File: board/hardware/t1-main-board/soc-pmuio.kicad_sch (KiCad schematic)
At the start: 28 parts, among them U1301 RK3566, Y1301 24 MHz

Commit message: Board: capture blk.debug
Debug UART2 (1.8 V) and I2S/DSD pads with ground pads, reset, PMIC and
power-key pads (PCB-T-09), a pad on every spare SoC GPIO whose pinout v1
row names one (the DEBUG bus, on the SoC's right edge), and a rail pad
for each power-tree rail no other sheet probes (PCB-T-02). Each DAC
sheet carries a pad on its MCLK. The spares pinout v1 leaves without a
pad now carry no-connect flags. On the root, facing sheet pins are
joined directly only where the route meets no other symbol.

Co-Authored-By: Claude Opus 5.5 <noreply@anthropic.com>
Claude-Session: https://claude.ai/code/session_01Ei262h3TpgY9vyfNLMi5Mn
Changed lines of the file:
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@@
 (label "EFUSE_VBUS_IMON" (at 132.08 203.2 90) (effects (font (size 1.27 1.27)) (justify left bottom)))
 (bus (pts (xy 45.72 252.73) (xy 50.8 252.73)) (stroke (width 0) (type default)))
-(hierarchical_label "{FP}" (shape bidirectional) (at 45.72 252.73 180) (effects (font (size 1.27 1.27)) (justify right)))
+(hierarchical_label "{DEBUG}" (shape bidirectional) (at 45.72 252.73 180) (effects (font (size 1.27 1.27)) (justify right)))
 (bus (pts (xy 76.2 252.73) (xy 81.28 252.73)) (stroke (width 0) (type default)))
-(hierarchical_label "{I2C0}" (shape bidirectional) (at 76.2 252.73 180) (effects (font (size 1.27 1.27)) (justify right)))
+(hierarchical_label "{FP}" (shape bidirectional) (at 76.2 252.73 180) (effects (font (size 1.27 1.27)) (justify right)))
 (bus (pts (xy 106.68 252.73) (xy 111.76 252.73)) (stroke (width 0) (type default)))
-(hierarchical_label "{I2C1}" (shape bidirectional) (at 106.68 252.73 180) (effects (font (size 1.27 1.27)) (justify right)))
+(hierarchical_label "{I2C0}" (shape bidirectional) (at 106.68 252.73 180) (effects (font (size 1.27 1.27)) (justify right)))
 (bus (pts (xy 137.16 252.73) (xy 142.24 252.73)) (stroke (width 0) (type default)))
-(hierarchical_label "{I2C2}" (shape bidirectional) (at 137.16 252.73 180) (effects (font (size 1.27 1.27)) (justify right)))
+(hierarchical_label "{I2C1}" (shape bidirectional) (at 137.16 252.73 180) (effects (font (size 1.27 1.27)) (justify right)))
 (bus (pts (xy 167.64 252.73) (xy 172.72 252.73)) (stroke (width 0) (type default)))
-(hierarchical_label "{IMON}" (shape bidirectional) (at 167.64 252.73 180) (effects (font (size 1.27 1.27)) (justify right)))
+(hierarchical_label "{I2C2}" (shape bidirectional) (at 167.64 252.73 180) (effects (font (size 1.27 1.27)) (justify right)))
 (bus (pts (xy 198.12 252.73) (xy 203.2 252.73)) (stroke (width 0) (type default)))
-(hierarchical_label "{IO_IRQ}" (shape bidirectional) (at 198.12 252.73 180) (effects (font (size 1.27 1.27)) (justify right)))
+(hierarchical_label "{IMON}" (shape bidirectional) (at 198.12 252.73 180) (effects (font (size 1.27 1.27)) (justify right)))
 (bus (pts (xy 228.6 252.73) (xy 233.68 252.73)) (stroke (width 0) (type default)))
-(hierarchical_label "{KEYS}" (shape bidirectional) (at 228.6 252.73 180) (effects (font (size 1.27 1.27)) (justify right)))
+(hierarchical_label "{IO_IRQ}" (shape bidirectional) (at 228.6 252.73 180) (effects (font (size 1.27 1.27)) (justify right)))
 (bus (pts (xy 259.08 252.73) (xy 264.16 252.73)) (stroke (width 0) (type default)))
-(hierarchical_label "{NFC}" (shape bidirectional) (at 259.08 252.73 180) (effects (font (size 1.27 1.27)) (justify right)))
+(hierarchical_label "{KEYS}" (shape bidirectional) (at 259.08 252.73 180) (effects (font (size 1.27 1.27)) (justify right)))
 (bus (pts (xy 45.72 245.11) (xy 50.8 245.11)) (stroke (width 0) (type default)))
-(hierarchical_label "{PMIC_CTL}" (shape bidirectional) (at 45.72 245.11 180) (effects (font (size 1.27 1.27)) (justify right)))
+(hierarchical_label "{NFC}" (shape bidirectional) (at 45.72 245.11 180) (effects (font (size 1.27 1.27)) (justify right)))
 (bus (pts (xy 76.2 245.11) (xy 81.28 245.11)) (stroke (width 0) (type default)))
-(hierarchical_label "{RP}" (shape bidirectional) (at 76.2 245.11 180) (effects (font (size 1.27 1.27)) (justify right)))
+(hierarchical_label "{PMIC_CTL}" (shape bidirectional) (at 76.2 245.11 180) (effects (font (size 1.27 1.27)) (justify right)))
 (bus (pts (xy 106.68 245.11) (xy 111.76 245.11)) (stroke (width 0) (type default)))
-(hierarchical_label "{SDMMC0}" (shape bidirectional) (at 106.68 245.11 180) (effects (font (size 1.27 1.27)) (justify right)))
+(hierarchical_label "{RP}" (shape bidirectional) (at 106.68 245.11 180) (effects (font (size 1.27 1.27)) (justify right)))
 (bus (pts (xy 137.16 245.11) (xy 142.24 245.11)) (stroke (width 0) (type default)))
-(hierarchical_label "{TPM}" (shape bidirectional) (at 137.16 245.11 180) (effects (font (size 1.27 1.27)) (justify right)))
+(hierarchical_label "{SDMMC0}" (shape bidirectional) (at 137.16 245.11 180) (effects (font (size 1.27 1.27)) (justify right)))
 (bus (pts (xy 167.64 245.11) (xy 172.72 245.11)) (stroke (width 0) (type default)))
-(hierarchical_label "{WL}" (shape bidirectional) (at 167.64 245.11 180) (effects (font (size 1.27 1.27)) (justify right)))
+(hierarchical_label "{TPM}" (shape bidirectional) (at 167.64 245.11 180) (effects (font (size 1.27 1.27)) (justify right)))
+(bus (pts (xy 198.12 245.11) (xy 203.2 245.11)) (stroke (width 0) (type default)))
+(hierarchical_label "{WL}" (shape bidirectional) (at 198.12 245.11 180) (effects (font (size 1.27 1.27)) (justify right)))
 (embedded_fonts no))

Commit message: Board: capture blk.cover-detect
COVER_DET_N on GPIO0_A6 (AJ38, PMUIO1, wake-capable), recorded in
pinout v1 (closes feature blocks G22): board-edge input and ground pads
for the case's actuator, 100 kΩ to vcc3v3_pmu, TPD1E10B06 at the pad
(BOM v1 line 143, PCB-L-10). The line rides the KEYS bus with the
buttons.

Co-Authored-By: Claude Opus 5.5 <noreply@anthropic.com>
Claude-Session: https://claude.ai/code/session_01Ei262h3TpgY9vyfNLMi5Mn
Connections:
- net SPARE_0A6 renamed COVER_DET_N
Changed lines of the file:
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@@
 (label "NFC_IRQ" (at 41.91 52.07 180) (effects (font (size 1.27 1.27)) (justify right bottom)))
 (label "EXP_INT_N" (at 41.91 54.61 180) (effects (font (size 1.27 1.27)) (justify right bottom)))
-(label "SPARE_0A6" (at 41.91 57.15 180) (effects (font (size 1.27 1.27)) (justify right bottom)))
+(label "COVER_DET_N" (at 41.91 57.15 180) (effects (font (size 1.27 1.27)) (justify right bottom)))
 (label "PMIC_SLEEP" (at 41.91 59.69 180) (effects (font (size 1.27 1.27)) (justify right bottom)))
 (label "FP_HID_INT_N" (at 41.91 62.23 180) (effects (font (size 1.27 1.27)) (justify right bottom)))

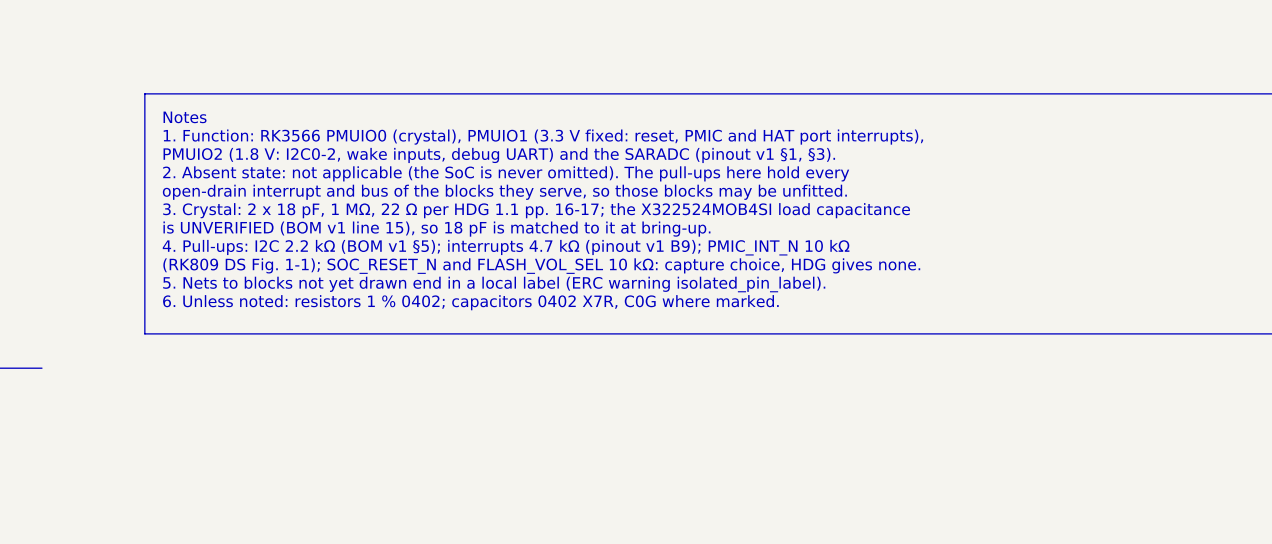
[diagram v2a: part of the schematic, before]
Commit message: Board: capture blk.maskrom
Power + Vol- at a cold power-on pull eMMC D0 low inside the TPS3808G01
boot window (BOM v1 lines 35, 78, 97, 98; sim/maskrom): SENSE 280k/100k,
CT 390 nF, WINDOW_N with its pad, SN74LVC1G57 and SN74LVC1G58 on
vcca1v8_pmu, BAT54 from PWRON_N, DMG1012T through 1 kΩ to EMMC_D0.
Every block in use now has its sheet; the README states the remaining
single-pin nets.

Co-Authored-By: Claude Opus 5.5 <noreply@anthropic.com>
Claude-Session: https://claude.ai/code/session_01Ei262h3TpgY9vyfNLMi5Mn
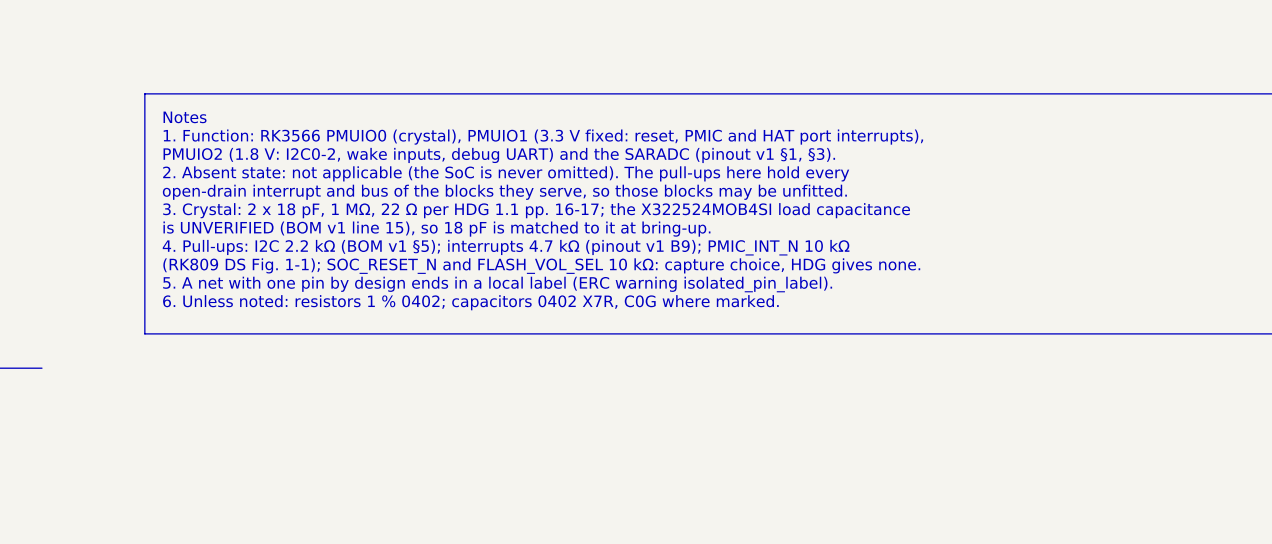
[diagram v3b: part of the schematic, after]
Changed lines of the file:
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@@
   (instances (project "t1-main-board" (path "/7746052e-d7f9-59ad-ba73-bd2b74439529/8302eaa7-1fc9-5a34-8a84-8a9171d22bdf/ab44a32b-0265-5973-a10e-b5131ba8c500" (reference "#PWR0200") (unit 1))))
 )
-(text_box "Notes\n1. Function: RK3566 PMUIO0 (crystal), PMUIO1 (3.3 V fixed: reset, PMIC and HAT port interrupts),\n   PMUIO2 (1.8 V: I2C0-2, wake inputs, debug UART) and the SARADC (pinout v1 §1, §3).\n2. Absent state: not applicable (the SoC is never omitted). The pull-ups here hold every\n   open-drain interrupt and bus of the blocks they serve, so those blocks may be unfitted.\n3. Crystal: 2 x 18 pF, 1 MΩ, 22 Ω per HDG 1.1 pp. 16-17; the X322524MOB4SI load capacitance\n   is UNVERIFIED (BOM v1 line 15), so 18 pF is matched to it at bring-up.\n4. Pull-ups: I2C 2.2 kΩ (BOM v1 §5); interrupts 4.7 kΩ (pinout v1 B9); PMIC_INT_N 10 kΩ\n   (RK809 DS Fig. 1-1); SOC_RESET_N and FLASH_VOL_SEL 10 kΩ: capture choice, HDG gives none.\n5. Nets to blocks not yet drawn end in a local label (ERC warning isolated_pin_label).\n6. Unless noted: resistors 1 % 0402; capacitors 0402 X7R, C0G where marked." (exclude_from_sim no) (at 275.59 222.25 0) (size 129.54 26.67) (margins 1.905 1.905 1.905 1.905) (stroke (width 0) (type default)) (fill (type none)) (effects (font (size 1.27 1.27)) (justify left top)))
+(text_box "Notes\n1. Function: RK3566 PMUIO0 (crystal), PMUIO1 (3.3 V fixed: reset, PMIC and HAT port interrupts),\n   PMUIO2 (1.8 V: I2C0-2, wake inputs, debug UART) and the SARADC (pinout v1 §1, §3).\n2. Absent state: not applicable (the SoC is never omitted). The pull-ups here hold every\n   open-drain interrupt and bus of the blocks they serve, so those blocks may be unfitted.\n3. Crystal: 2 x 18 pF, 1 MΩ, 22 Ω per HDG 1.1 pp. 16-17; the X322524MOB4SI load capacitance\n   is UNVERIFIED (BOM v1 line 15), so 18 pF is matched to it at bring-up.\n4. Pull-ups: I2C 2.2 kΩ (BOM v1 §5); interrupts 4.7 kΩ (pinout v1 B9); PMIC_INT_N 10 kΩ\n   (RK809 DS Fig. 1-1); SOC_RESET_N and FLASH_VOL_SEL 10 kΩ: capture choice, HDG gives none.\n5. A net with one pin by design ends in a local label (ERC warning isolated_pin_label).\n6. Unless noted: resistors 1 % 0402; capacitors 0402 X7R, C0G where marked." (exclude_from_sim no) (at 275.59 222.25 0) (size 129.54 26.67) (margins 1.905 1.905 1.905 1.905) (stroke (width 0) (type default)) (fill (type none)) (effects (font (size 1.27 1.27)) (justify left top)))
 (text "Rails" (exclude_from_sim no) (at 22.86 269.24 0) (effects (font (size 2.54 2.54)) (justify left bottom)))
 (table (column_count 3) (border (external yes) (header yes) (stroke (width 0) (type solid))) (separators (rows yes) (cols yes) (stroke (width 0) (type solid))) (column_widths 27.94 78.74 138.43) (row_heights 5.08 5.08) (cells (table_cell "Rail" (exclude_from_sim no) (at 22.86 270.51 0) (size 27.94 5.08) (margins 0.9525 0.9525 0.9525 0.9525) (span 1 1) (fill (type none)) (effects (font (size 1.27 1.27) (bold yes)) (justify left top))) (table_cell "Capacitors" (exclude_from_sim no) (at 50.8 270.51 0) (size 78.74 5.08) (margins 0.9525 0.9525 0.9525 0.9525) (span 1 1) (fill (type none)) (effects (font (size 1.27 1.27) (bold yes)) (justify left top))) (table_cell "Requirement and source" (exclude_from_sim no) (at 129.54 270.51 0) (size 138.43 5.08) (margins 0.9525 0.9525 0.9525 0.9525) (span 1 1) (fill (type none)) (effects (font (size 1.27 1.27) (bold yes)) (justify left top))) (table_cell "vcca_1v8" (exclude_from_sim no) (at 22.86 275.59 0) (size 27.94 5.08) (margins 0.9525 0.9525 0.9525 0.9525) (span 1 1) (fill (type none)) (effects (font (size 1.27 1.27)) (justify left top))) (table_cell "4 x 1 nF on VIN0-VIN3" (exclude_from_sim no) (at 50.8 275.59 0) (size 78.74 5.08) (margins 0.9525 0.9525 0.9525 0.9525) (span 1 1) (fill (type none)) (effects (font (size 1.27 1.27)) (justify left top))) (table_cell "1 nF per input; 10 kΩ on VIN0 (HDG 1.1 p. 60)" (exclude_from_sim no) (at 129.54 275.59 0) (size 138.43 5.08) (margins 0.9525 0.9525 0.9525 0.9525) (span 1 1) (fill (type none)) (effects (font (size 1.27 1.27)) (justify left top)))))

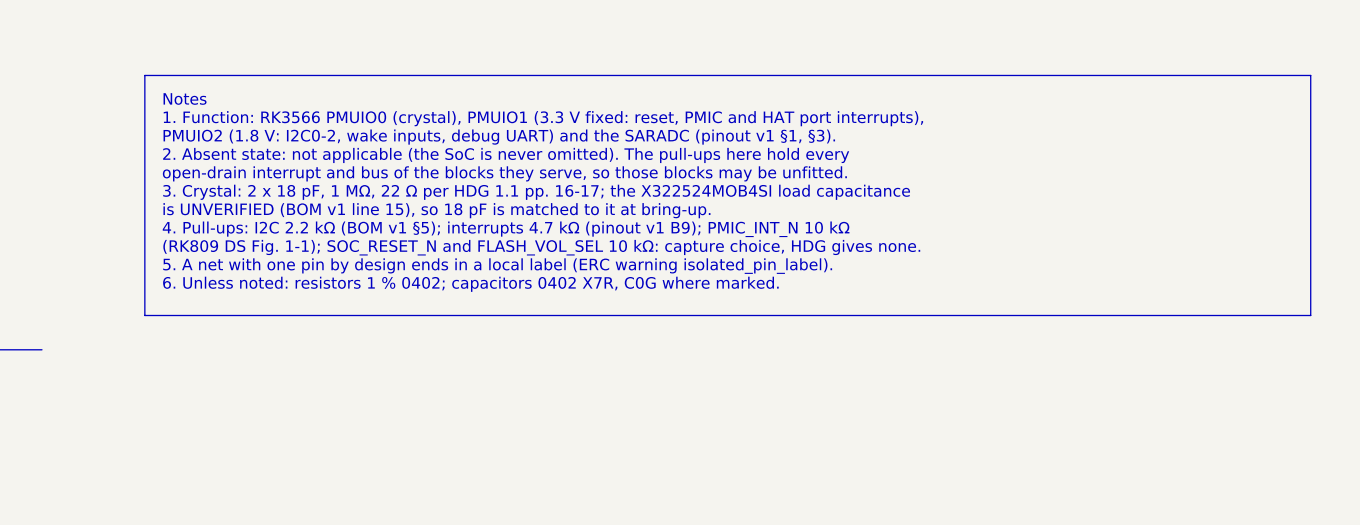
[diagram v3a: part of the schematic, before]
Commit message: Compaction: lower inductors, 0201 decoupling, 0.8 mm signal test pads
A matrix tool (hardware/studies/compaction) checks each candidate against
the design's stresses: same inductance, design peak <= 70 % and the
converter's maximum limit <= 100 % of Isat (30 % drop), height zones,
ratings at least twice the rail, PCB-D-06; sourcing outcome per part.

Applied (placement v1 decision 12, BOM v1.15):
- L601, L4401: XGL4015-102MEC (1.5 mm) for XAL/XGL4020-102MEC (2.1 mm);
- L1001, L5101: XGL4015-471MEC (1.5 mm) for Wurth 744373240047, on the
  stock XxL4020 land (the Wurth land was never drawn);
- L1201 is 1.2 mm (XGL4012, per-MPN heights): it moves next to the SoC;
- 58 x 100 nF decoupling on rails <= 3.3 V in core/IO/radio: 0201;
- 51 test pads on signal nets: 0.8 mm (PCB-D-06 v0.16, JLCPCB guide).
Kept: L901, L2802 (XGL4015 at 103 % of Isat at the limit); no thinner
0805/1206 capacitor passes (obsolete, NRND or unlisted).

Board need 113 % -> 111 % (core band 227 -> 203 %, power band 258 ->
233 %, radio band 19 -> 0 %); only C904 still relies on PCB-Z-04.
ERC 0 errors, craft Q1 met, DRC 0 errors (605 warnings), pcb and study
tests pass, rules test board PASS.

Co-Authored-By: Claude Opus 5.5 <noreply@anthropic.com>
Claude-Session: https://claude.ai/code/session_01Ei262h3TpgY9vyfNLMi5Mn
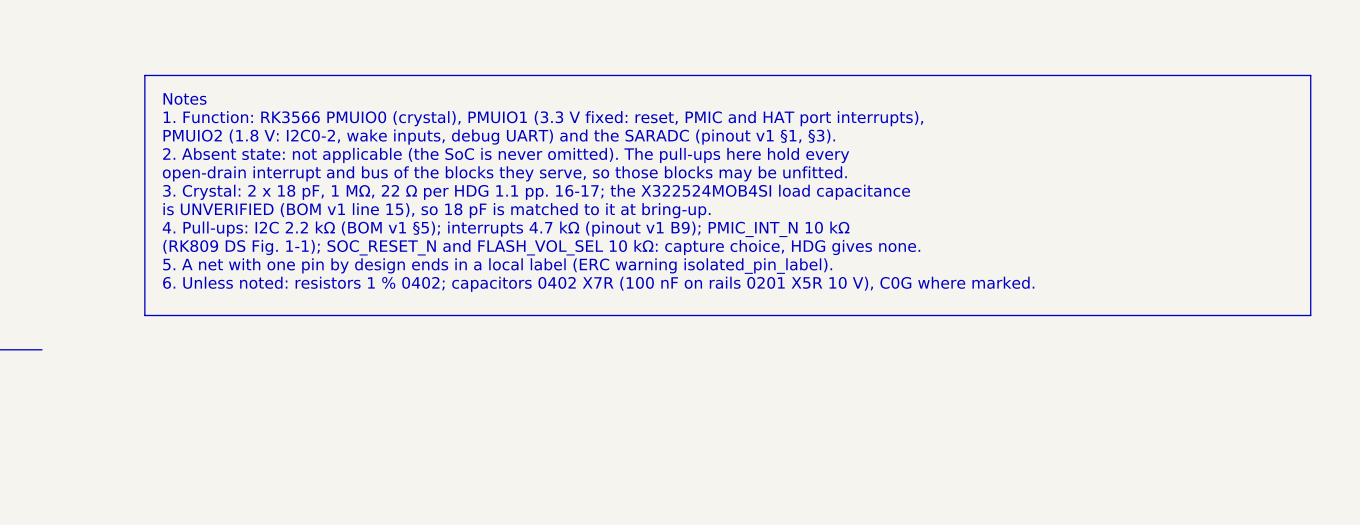
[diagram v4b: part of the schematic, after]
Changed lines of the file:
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@@
   (instances (project "t1-main-board" (path "/7746052e-d7f9-59ad-ba73-bd2b74439529/8302eaa7-1fc9-5a34-8a84-8a9171d22bdf/ab44a32b-0265-5973-a10e-b5131ba8c500" (reference "#PWR0200") (unit 1))))
 )
-(text_box "Notes\n1. Function: RK3566 PMUIO0 (crystal), PMUIO1 (3.3 V fixed: reset, PMIC and HAT port interrupts),\n   PMUIO2 (1.8 V: I2C0-2, wake inputs, debug UART) and the SARADC (pinout v1 §1, §3).\n2. Absent state: not applicable (the SoC is never omitted). The pull-ups here hold every\n   open-drain interrupt and bus of the blocks they serve, so those blocks may be unfitted.\n3. Crystal: 2 x 18 pF, 1 MΩ, 22 Ω per HDG 1.1 pp. 16-17; the X322524MOB4SI load capacitance\n   is UNVERIFIED (BOM v1 line 15), so 18 pF is matched to it at bring-up.\n4. Pull-ups: I2C 2.2 kΩ (BOM v1 §5); interrupts 4.7 kΩ (pinout v1 B9); PMIC_INT_N 10 kΩ\n   (RK809 DS Fig. 1-1); SOC_RESET_N and FLASH_VOL_SEL 10 kΩ: capture choice, HDG gives none.\n5. A net with one pin by design ends in a local label (ERC warning isolated_pin_label).\n6. Unless noted: resistors 1 % 0402; capacitors 0402 X7R, C0G where marked." (exclude_from_sim no) (at 275.59 222.25 0) (size 129.54 26.67) (margins 1.905 1.905 1.905 1.905) (stroke (width 0) (type default)) (fill (type none)) (effects (font (size 1.27 1.27)) (justify left top)))
+(text_box "Notes\n1. Function: RK3566 PMUIO0 (crystal), PMUIO1 (3.3 V fixed: reset, PMIC and HAT port interrupts),\n   PMUIO2 (1.8 V: I2C0-2, wake inputs, debug UART) and the SARADC (pinout v1 §1, §3).\n2. Absent state: not applicable (the SoC is never omitted). The pull-ups here hold every\n   open-drain interrupt and bus of the blocks they serve, so those blocks may be unfitted.\n3. Crystal: 2 x 18 pF, 1 MΩ, 22 Ω per HDG 1.1 pp. 16-17; the X322524MOB4SI load capacitance\n   is UNVERIFIED (BOM v1 line 15), so 18 pF is matched to it at bring-up.\n4. Pull-ups: I2C 2.2 kΩ (BOM v1 §5); interrupts 4.7 kΩ (pinout v1 B9); PMIC_INT_N 10 kΩ\n   (RK809 DS Fig. 1-1); SOC_RESET_N and FLASH_VOL_SEL 10 kΩ: capture choice, HDG gives none.\n5. A net with one pin by design ends in a local label (ERC warning isolated_pin_label).\n6. Unless noted: resistors 1 % 0402; capacitors 0402 X7R (100 nF on rails 0201 X5R 10 V), C0G where marked." (exclude_from_sim no) (at 275.59 222.25 0) (size 129.54 26.67) (margins 1.905 1.905 1.905 1.905) (stroke (width 0) (type default)) (fill (type none)) (effects (font (size 1.27 1.27)) (justify left top)))
 (text "Rails" (exclude_from_sim no) (at 22.86 269.24 0) (effects (font (size 2.54 2.54)) (justify left bottom)))
 (table (column_count 3) (border (external yes) (header yes) (stroke (width 0) (type solid))) (separators (rows yes) (cols yes) (stroke (width 0) (type solid))) (column_widths 27.94 78.74 138.43) (row_heights 5.08 5.08) (cells (table_cell "Rail" (exclude_from_sim no) (at 22.86 270.51 0) (size 27.94 5.08) (margins 0.9525 0.9525 0.9525 0.9525) (span 1 1) (fill (type none)) (effects (font (size 1.27 1.27) (bold yes)) (justify left top))) (table_cell "Capacitors" (exclude_from_sim no) (at 50.8 270.51 0) (size 78.74 5.08) (margins 0.9525 0.9525 0.9525 0.9525) (span 1 1) (fill (type none)) (effects (font (size 1.27 1.27) (bold yes)) (justify left top))) (table_cell "Requirement and source" (exclude_from_sim no) (at 129.54 270.51 0) (size 138.43 5.08) (margins 0.9525 0.9525 0.9525 0.9525) (span 1 1) (fill (type none)) (effects (font (size 1.27 1.27) (bold yes)) (justify left top))) (table_cell "vcca_1v8" (exclude_from_sim no) (at 22.86 275.59 0) (size 27.94 5.08) (margins 0.9525 0.9525 0.9525 0.9525) (span 1 1) (fill (type none)) (effects (font (size 1.27 1.27)) (justify left top))) (table_cell "4 x 1 nF on VIN0-VIN3" (exclude_from_sim no) (at 50.8 275.59 0) (size 78.74 5.08) (margins 0.9525 0.9525 0.9525 0.9525) (span 1 1) (fill (type none)) (effects (font (size 1.27 1.27)) (justify left top))) (table_cell "1 nF per input; 10 kΩ on VIN0 (HDG 1.1 p. 60)" (exclude_from_sim no) (at 129.54 275.59 0) (size 138.43 5.08) (margins 0.9525 0.9525 0.9525 0.9525) (span 1 1) (fill (type none)) (effects (font (size 1.27 1.27)) (justify left top)))))
